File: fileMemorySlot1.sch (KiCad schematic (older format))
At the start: 4 parts, among them J10 MM1_addressExtension, J8 MM1_receptacle_5530843-2

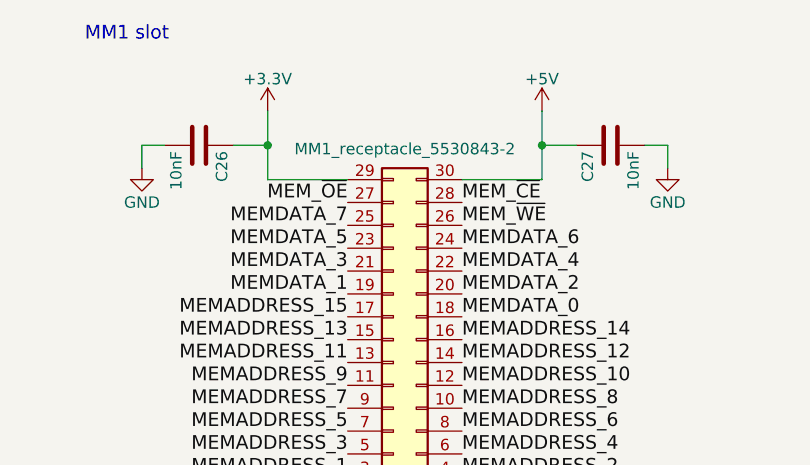
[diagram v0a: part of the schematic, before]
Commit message: Better decoupling
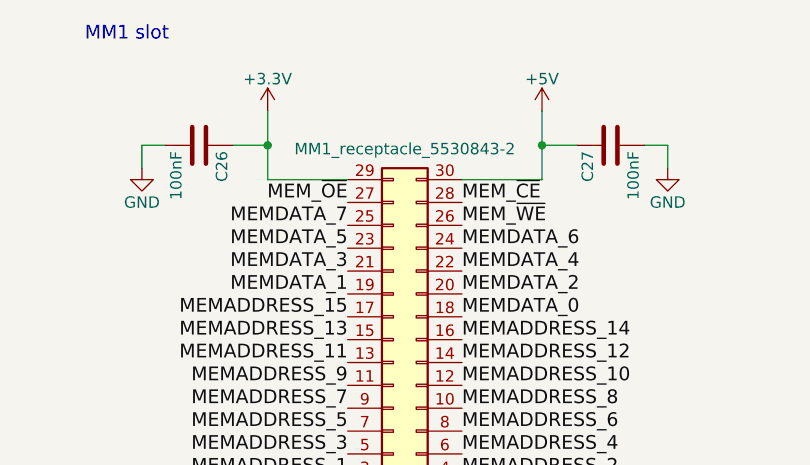
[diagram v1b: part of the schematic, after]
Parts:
- C26, C27: value 10nF -> 100nF
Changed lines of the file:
@@
 AR Path="/5E0692F0/5D5B8D60" Ref="C?"  Part="1"
 F 0 "C26" H 5825 1400 50  0000 L CNN
-F 1 "10nF" H 5825 1200 50  0000 L CNN
+F 1 "100nF" H 5825 1200 50  0000 L CNN
 F 2 "Capacitor_SMD:C_0805_2012Metric" H 5838 1150 50  0001 C CNN
 F 3 "" H 5800 1300 50  0001 C CNN
@@
 AR Path="/5E0692F0/5D5B8D61" Ref="C?"  Part="1"
 F 0 "C27" H 7625 1400 50  0000 L CNN
-F 1 "10nF" H 7625 1200 50  0000 L CNN
+F 1 "100nF" H 7625 1200 50  0000 L CNN
 F 2 "Capacitor_SMD:C_0805_2012Metric" H 7638 1150 50  0001 C CNN
 F 3 "" H 7600 1300 50  0001 C CNN
